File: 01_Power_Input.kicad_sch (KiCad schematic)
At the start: 9 parts, among them J1 J_BAT_3S2P, Q1 SQJQ100E, U1 LM74700

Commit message: 02_Servo_Power in progress
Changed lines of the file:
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@@
 		(color 0 0 0 0)
 	)
+	(junction
+		(at 138.43 99.06)
+		(diameter 0)
+		(color 0 0 0 0)
+	)
 	(wire
 		(pts
@@
 	(wire
 		(pts
+			(xy 138.43 99.06) (xy 138.43 105.41)
+		)
+		(stroke
+			(width 0)
+			(type default)
+		)
+	)
+	(wire
+		(pts
 			(xy 116.84 91.44) (xy 123.19 91.44)
 		)
@@
 	(wire
 		(pts
-			(xy 138.43 96.52) (xy 138.43 105.41)
+			(xy 138.43 96.52) (xy 138.43 99.06)
 		)
 		(stroke
@@
 		(pts
 			(xy 133.35 91.44) (xy 138.43 91.44)
+		)
+		(stroke
+			(width 0)
+			(type default)
+		)
+	)
+	(wire
+		(pts
+			(xy 138.43 99.06) (xy 139.7 99.06)
 		)
 		(stroke
@@
 		)
 	)
+	(hierarchical_label "VBAT_PROT"
+		(shape input)
+		(at 139.7 99.06 0)
+		(effects
+			(font
+				(size 1.27 1.27)
+			)
+			(justify left)
+		)
+	)

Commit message: added footprints R and C and more
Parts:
- C1, C2, C3, C4: footprint (none) -> Capacitor_SMD:C_0805_2012Metric_Pad1.18x1.45mm_HandSolder
- F1: footprint (none) -> Fuse:Fuse_0805_2012Metric_Pad1.15x1.40mm_HandSolder
- J1: footprint (none) -> Connector_JST:JST_EH_B2B-EH-A_1x02_P2.50mm_Vertical
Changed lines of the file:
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@@
 			)
 		)
-		(property "Footprint" ""
+		(property "Footprint" "Capacitor_SMD:C_0805_2012Metric_Pad1.18x1.45mm_HandSolder"
 			(at 153.3652 68.58 0)
 			(hide yes)
@@
 			)
 		)
-		(property "Footprint" ""
+		(property "Footprint" "Capacitor_SMD:C_0805_2012Metric_Pad1.18x1.45mm_HandSolder"
 			(at 135.5852 113.03 0)
 			(hide yes)
@@
 			)
 		)
-		(property "Footprint" ""
+		(property "Footprint" "Capacitor_SMD:C_0805_2012Metric_Pad1.18x1.45mm_HandSolder"
 			(at 112.7252 113.03 0)
 			(hide yes)
@@
 			)
 		)
-		(property "Footprint" ""
+		(property "Footprint" "Capacitor_SMD:C_0805_2012Metric_Pad1.18x1.45mm_HandSolder"
 			(at 124.1552 113.03 0)
 			(hide yes)
@@
 			)
 		)
-		(property "Footprint" ""
+		(property "Footprint" "Connector_JST:JST_EH_B2B-EH-A_1x02_P2.50mm_Vertical"
 			(at 74.93 91.44 0)
 			(hide yes)
@@
 			)
 		)
-		(property "Footprint" ""
+		(property "Footprint" "Fuse:Fuse_0805_2012Metric_Pad1.15x1.40mm_HandSolder"
 			(at 101.6 93.218 90)
 			(hide yes)

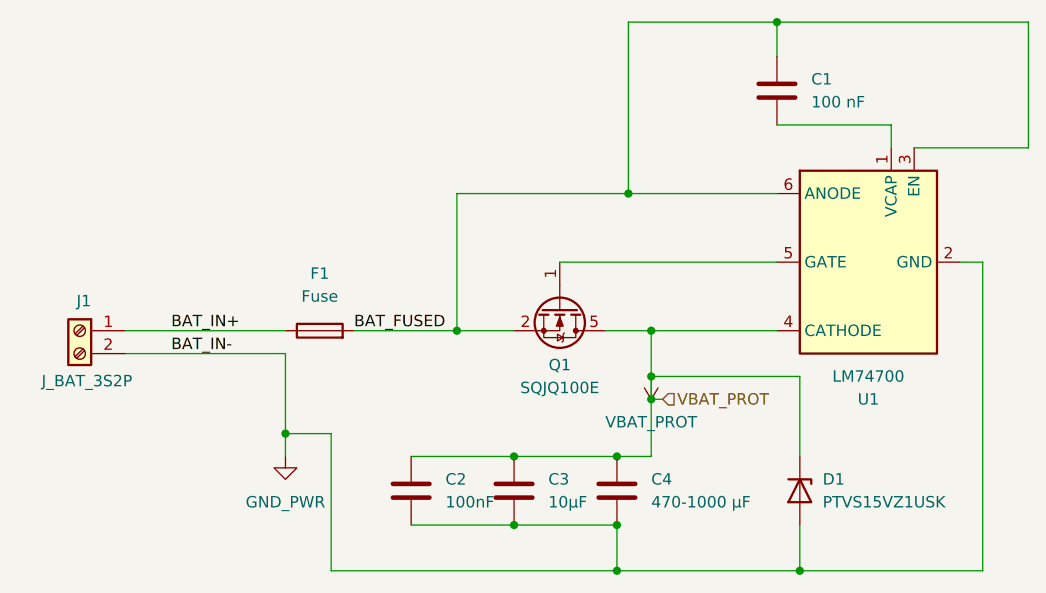
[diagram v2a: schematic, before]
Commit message: added 5v buck converter and place JST PH connectors
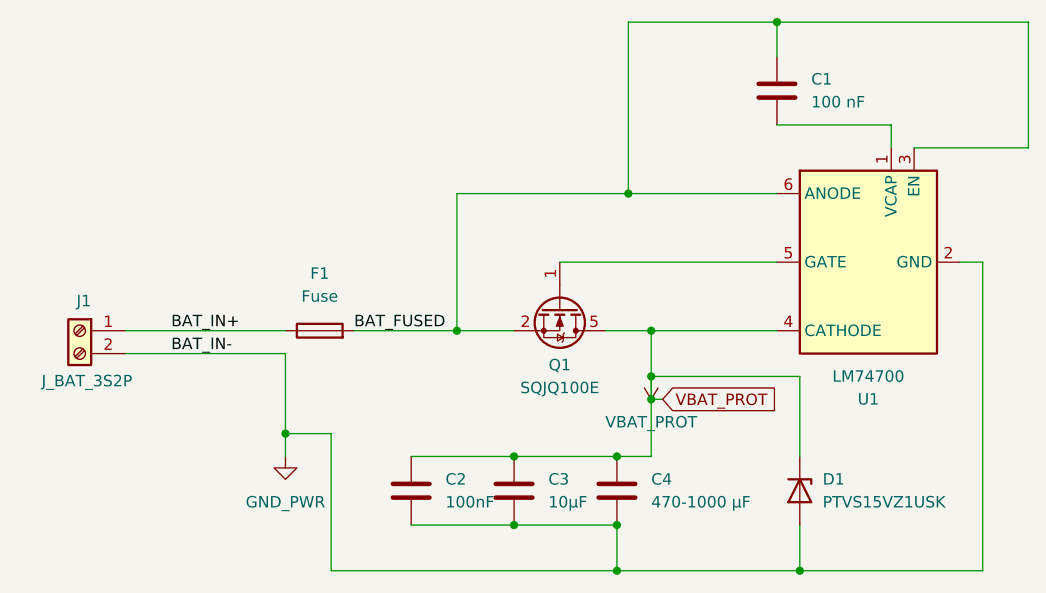
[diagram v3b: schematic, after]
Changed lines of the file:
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@@
 		)
 	)
-	(hierarchical_label "VBAT_PROT"
+	(global_label "VBAT_PROT"
 		(shape input)
 		(at 139.7 99.06 0)
+		(fields_autoplaced yes)
 		(effects
 			(font
@@
 			(justify left)
 		)
+		(property "Intersheetrefs" "${INTERSHEET_REFS}"
+			(at 152.9057 99.06 0)
+			(hide yes)
+			(show_name no)
+			(do_not_autoplace no)
+			(effects
+				(font
+					(size 1.27 1.27)
+				)
+				(justify left)
+			)
+		)
 	)

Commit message: added for 3v3 and 5v capacitors, resistors and induction footprints
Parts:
- C1, C2: footprint Capacitor_SMD:C_0805_2012Metric_Pad1.18x1.45mm_HandSolder -> C1608X7R1H474K080AC:CAPC1608X90N
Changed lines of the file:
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@@
 			)
 		)
-		(property "Footprint" "Capacitor_SMD:C_0805_2012Metric_Pad1.18x1.45mm_HandSolder"
+		(property "Footprint" "C1608X7R1H474K080AC:CAPC1608X90N"
 			(at 153.3652 68.58 0)
 			(hide yes)
@@
 			)
 		)
-		(property "Footprint" "Capacitor_SMD:C_0805_2012Metric_Pad1.18x1.45mm_HandSolder"
+		(property "Footprint" "C1608X7R1H474K080AC:CAPC1608X90N"
 			(at 112.7252 113.03 0)
 			(hide yes)

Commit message: change vbat_prot footprint and added pwrmux for 3v3 ubs_mcu connector
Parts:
- J1: footprint Connector_JST:JST_EH_B2B-EH-A_1x02_P2.50mm_Vertical -> TerminalBlock_Phoenix:TerminalBlock_Phoenix_MKDS-1,5-2-5.08_1x02_P5.08mm_Horizontal
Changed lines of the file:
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@@
 			)
 		)
-		(property "Footprint" "Connector_JST:JST_EH_B2B-EH-A_1x02_P2.50mm_Vertical"
+		(property "Footprint" "TerminalBlock_Phoenix:TerminalBlock_Phoenix_MKDS-1,5-2-5.08_1x02_P5.08mm_Horizontal"
 			(at 74.93 91.44 0)
 			(hide yes)
